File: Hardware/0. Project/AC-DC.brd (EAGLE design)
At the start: 100 x 74 mm, 90 parts, among them IC1 7824TV, IC2 7812TV, IC3 LM324D, IC4 LM358D, K1 12VDC COIL, K2 12VDC COIL, K3 12VDC COIL, K4 12VDC COIL, Q1 BC848SMD, Q2 BC848BSMD, Q3 BC858BSMD, Q4 BC858BSMD, Q5 BC858BSMD, Q6 BC858BSMD, U1 LM338K, U2 LM338K

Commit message: PCB layout done
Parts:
- added C16: 100nF x 50V, rcl:C0805
- moved R29 233.8 mm to (92.9, 39.5), flipped to the bottom, turned to 270 degrees
- moved R25 227.1 mm to (92.7, 33.2), flipped to the bottom, turned to 270 degrees
- moved D7 210.0 mm to (89.4, 41.9), flipped to the bottom
- moved Q3 208.2 mm to (84.5, 37.2), flipped to the bottom, turned to 180 degrees
- moved Q4 206.9 mm to (73.7, 35.2), flipped to the bottom, turned to 90 degrees
- moved R33 200.5 mm to (86.9, 33.2), flipped to the bottom, turned to 90 degrees
- moved R34 197.6 mm to (89.5, 33.1), flipped to the bottom, turned to 90 degrees
- moved R28 197.6 mm to (72.9, 39.6), flipped to the bottom, turned to 90 degrees
- moved C2 196.4 mm to (65.6, 45.6), flipped to the bottom, turned to 90 degrees
- moved R30 186.6 mm to (70.5, 39.7), flipped to the bottom, turned to 90 degrees
- moved D6 186.5 mm to (75.2, 32.3), flipped to the bottom, turned to 180 degrees
- moved R4 183.6 mm to (55.4, 30.3), flipped to the bottom, turned to 90 degrees
- moved C10 181.1 mm to (47.1, 49.3), flipped to the bottom, turned to 90 degrees
- moved IC4 177.6 mm to (63.3, 37.5), flipped to the bottom
- moved D9 173.3 mm to (39.0, 41.2), flipped to the bottom, turned to 90 degrees
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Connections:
- net +24V: now also C16.1
- net 0V: now also C16.2
- net SHORT_CIRCUIT_MONITOR_1: no longer AMP2.1, K3.11, VOLT2.P$3
- net SHORT_CIRCUIT_MONITOR_2: now also AMP2.1, K3.11, VOLT2.P$3
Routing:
- net +24V: track 0.00 -> 347.0 mm, vias 0 -> 2
- net 12V: track 0.00 -> 121.0 mm, vias 0 -> 4
- net SHORT_CIRCUIT_MONITOR_1: track 0.00 -> 114.6 mm, vias 0 -> 1
- net N$30: track 0.00 -> 98.5 mm, vias 0 -> 2
- net N$26: track 0.00 -> 91.3 mm
- net N$15: track 0.00 -> 89.3 mm
- net N$25: track 0.00 -> 87.7 mm, vias 0 -> 2
- net N$5: track 0.00 -> 86.6 mm, vias 0 -> 2
- net N$36: track 0.00 -> 84.2 mm, vias 0 -> 1
- net N$31: track 0.00 -> 76.8 mm
- net 30V_A: track 0.00 -> 75.4 mm
- net N$35: track 0.00 -> 73.8 mm, vias 0 -> 3
- net N$27: track 0.00 -> 71.0 mm, vias 0 -> 1
- net SHORT_CIRCUIT_MONITOR_2: track 0.00 -> 69.4 mm, vias 0 -> 1
- net 30V_B: track 0.00 -> 64.5 mm, vias 0 -> 1
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- added copper zone on layer 1, net 0V
- added copper zone on layer 16, net 0V
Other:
- board size 100 x 74 mm -> 100 x 75 mm
- board text added: "AMP1"
- board text added: "AMP2"
- board text added: "COOLER"
- board text added: "LED"
- board text added: "LM338"
- board text added: "OUT1"
- board text added: "OUT2"
- board text added: "POT1"
- board text added: "POT2"
- board text added: "SWITCH"
- board text added: "TEMP"
- board text added: "TRAFO 1"
- board text added: "TRAFO 2"
- board text added: "VOLT1"
- board text added: "VOLT2"

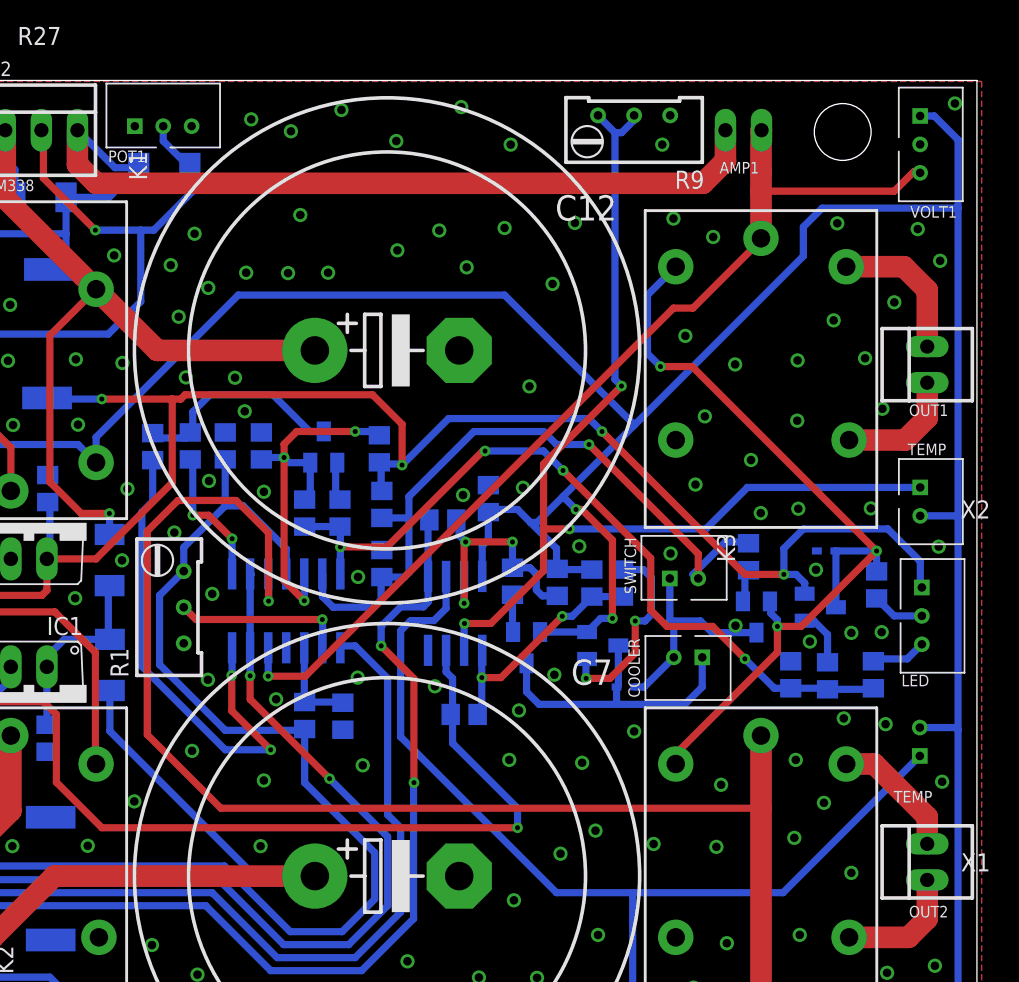
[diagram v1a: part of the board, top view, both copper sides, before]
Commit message: tStop added to high current traces
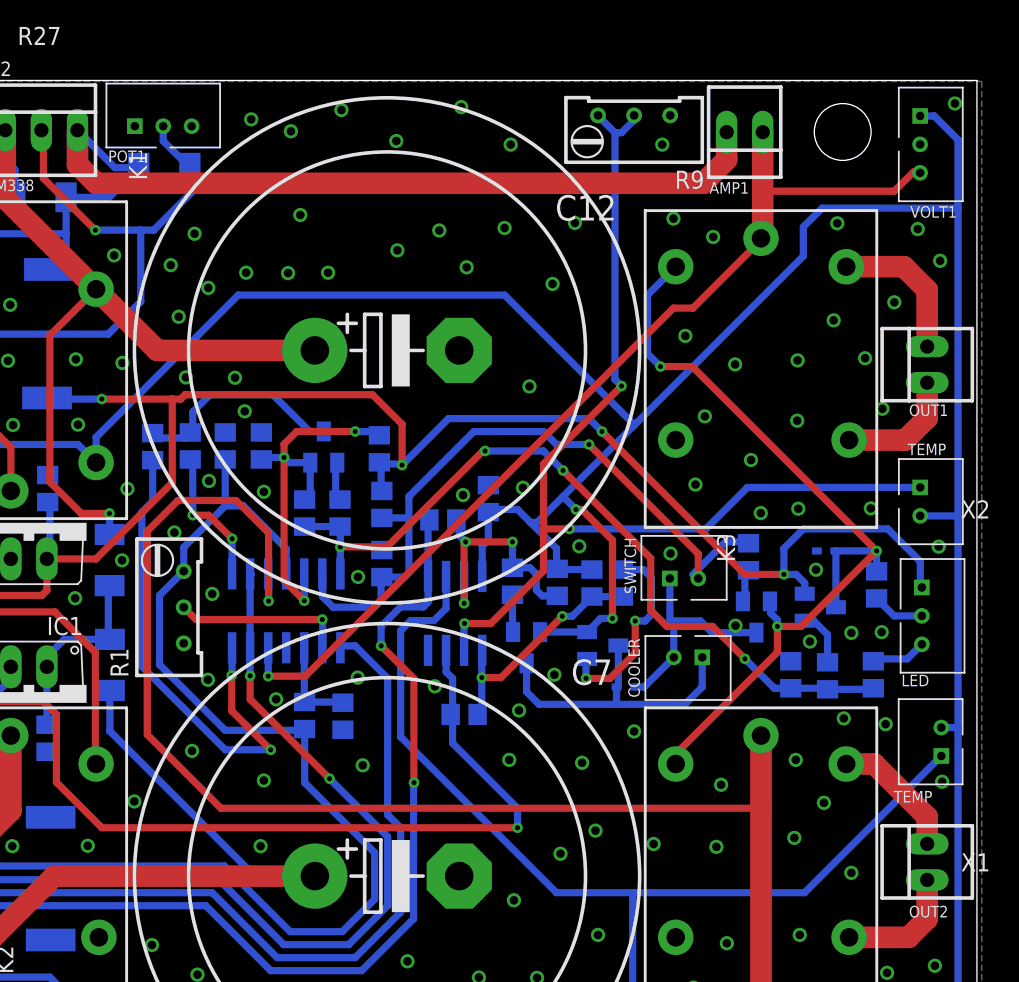
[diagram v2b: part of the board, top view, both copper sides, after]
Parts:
- moved RT3 1.51 mm to (97.5, 27.5), flipped to the top
- moved AMP2 0.16 mm to (83.7, 71.4), flipped to the top, turned to 180 degrees
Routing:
- net N$31: track 76.8 -> 78.3 mm
- net +24V: track 347.0 -> 345.7 mm
- net SHORT_CIRCUIT_MONITOR_2: track 69.4 -> 68.7 mm
